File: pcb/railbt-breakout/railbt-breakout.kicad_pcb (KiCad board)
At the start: 2 copper layers, 52.6 x 25.8 mm, 6 parts, among them J1 RJ45, J2 RJ45, Q1 BC108, U1 XL1509

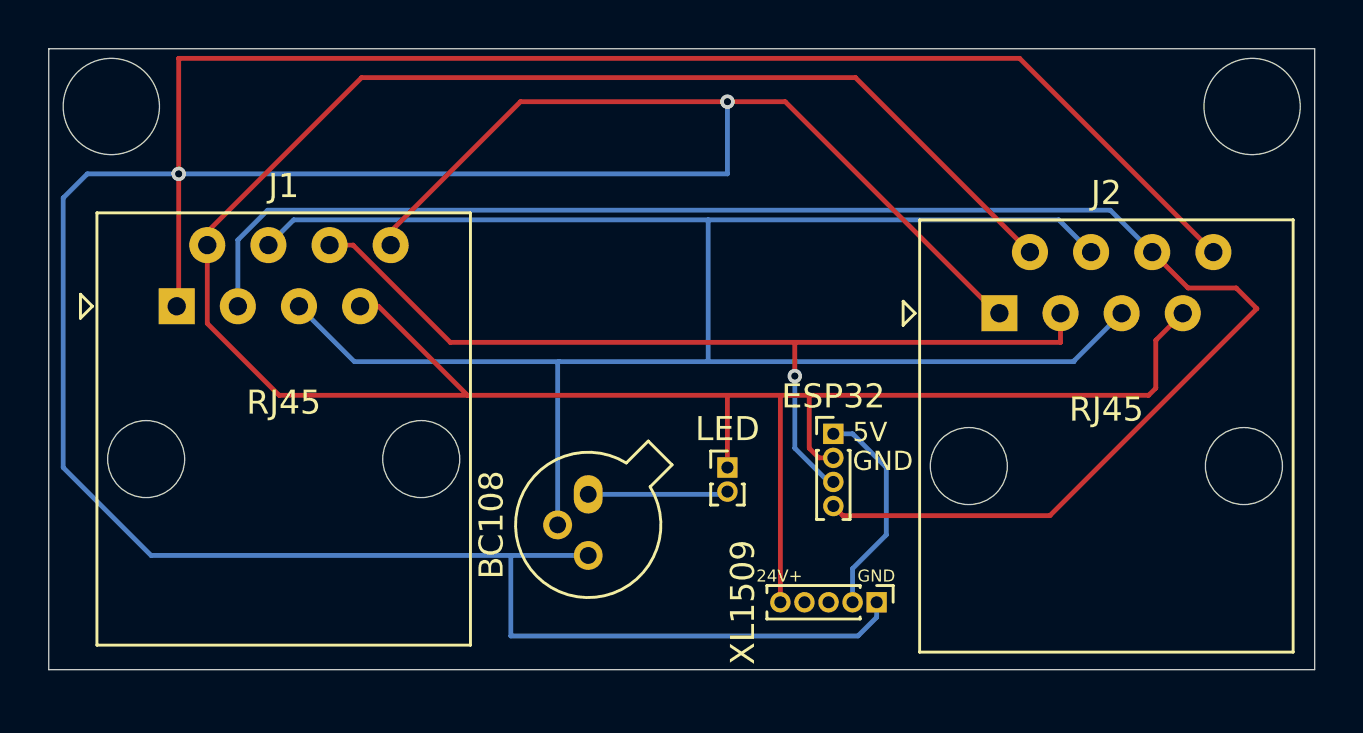
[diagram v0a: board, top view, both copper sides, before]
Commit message: Update PCB to latest revision
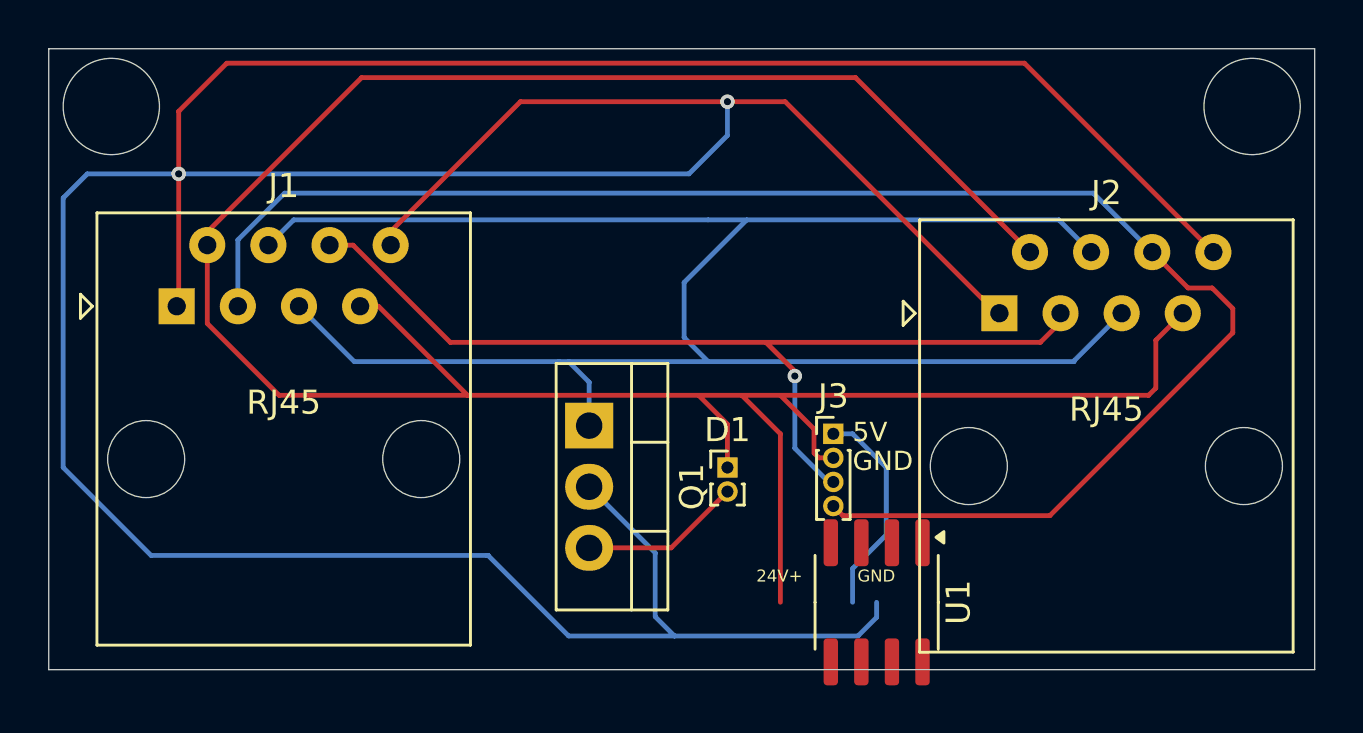
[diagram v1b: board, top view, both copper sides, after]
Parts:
- Q1: footprint Package_TO_SOT_THT:TO-18-3 -> Package_TO_SOT_THT:TO-220-3_Vertical
- U1: value XL1509 -> XL1509-5.0; footprint Connector_PinHeader_1.00mm:PinHeader_1x05_P1.00mm_Vertical -> Package_SO:SOIC-8_3.9x4.9mm_P1.27mm
- moved Q1 2.86 mm to (128.9, 59.9)
- renumbered ESP32 to J3
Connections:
- J1 pad 1: Net-(Q1-C) -> Net-(Q1-D)
- J1 pad 4: Net-(Q1-B) -> Net-(Q1-G)
- J1 pad 5: Net-(Q1-B) -> Net-(Q1-G)
- J1 pad 8: Net-(Q1-C) -> Net-(Q1-D)
- J2 pad 1: Net-(Q1-C) -> Net-(Q1-D)
- J2 pad 4: Net-(Q1-B) -> Net-(Q1-G)
- J2 pad 5: Net-(Q1-B) -> Net-(Q1-G)
- J2 pad 8: Net-(Q1-C) -> Net-(Q1-D)
- Q1 pad 1: Net-(D1-A) -> Net-(Q1-G)
- Q1 pad 2: Net-(Q1-B) -> Net-(Q1-D)
- Q1 pad 3: Net-(Q1-C) -> Net-(D1-A)
- U1 pad 1: Net-(Q1-C) -> Net-(Q1-D)
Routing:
- net Net-(Q1-D): track 0.00 -> 173.7 mm, vias 0 -> 2
- net Net-(Q1-C): track 173.5 -> 0.00 mm, vias 2 -> 0
- net Net-(Q1-B): track 83.9 -> 0.00 mm
- net Net-(Q1-G): track 0.00 -> 81.6 mm
- net Net-(D1-K): track 109.0 -> 110.6 mm
- net Net-(D1-A): track 5.83 -> 6.88 mm
- net Net-(J3-Pin_4): track 68.6 -> 67.8 mm
